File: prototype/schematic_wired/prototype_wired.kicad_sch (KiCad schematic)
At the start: 19 parts, among them J1 Conn4L, J10 LimitSwitch, J11 Conn4L, J2 Conn4L, J3 Conn4L, J4 EncoderSwitch, J5 EncoderSwitch, J6 EncoderSwitch, J7 Conn4L, J8 Conn4L, J9 LimitSwitch, U1 TMC2209-LA, U2 TMC2209-LA, U3 TMC2209-LA, U4 TCA9548A

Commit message: updates
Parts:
- removed ESP1: Conn11R, symbol Conn11R
- removed ESP2: Conn13L, symbol Conn13L
- removed J10, J9: LimitSwitch, symbol LimitSwitch
- removed J4, J5, J6: EncoderSwitch, symbol EncoderSwitch
- removed J7, J8: Conn4L, symbol Conn4L
- removed PWR1: Conn2L, symbol Conn2L
- removed U1, U2, U3: TMC2209-LA, symbol TMC2209-LA
- removed U4: TCA9548A, symbol TCA9548A
- added J12: oled, symbol Conn4L
- added J4, J5, J6: tmcA, symbol Connector_Generic:Conn_01x08
- added U1: TCA9548APWR, Package_SO:TSSOP-24_4.4x7.8mm_P0.65mm, symbol Interface_Expansion:TCA9548APWR
- added U5: ESP32-S3-DevKitC, PCM_Espressif:ESP32-S3-DevKitC, symbol PCM_Espressif:ESP32-S3-DevKitC
- J1: value Conn4L -> as5600_3
- J2: value Conn4L -> as5600_2
- J3: value Conn4L -> as5600_1
- renumbered ESP3 to 5v-in
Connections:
- new net: 5v-in.1, U5.21 (5V)
- new net: J3.1, U1.9 (SC2)
- new net: J3.2, U1.8 (SD2)
- new net: J1.3, J12.3, J2.3, J3.3, U1.24 (VCC), U1.3 (~{RESET}), U5.1 (3V3), U5.2 (3V3)
- new net: J1.4, J12.4, J2.4, J3.4, U1.1 (A0), U1.12 (GND), U1.2 (A1), U1.21 (A2), U5.22 (GND), U5.23 (GND), U5.24 (GND), U5.44 (GND)
- new net: J2.1, U1.7 (SC1)
- new net: J2.2, U1.6 (SD1)
- new net: J1.1, U1.5 (SC0)
- new net: J1.2, U1.4 (SD0)
- new net: J12.1, U5.20 (GPIO14/ADC2_CH3)
- new net: J12.2, U5.19 (GPIO13/ADC2_CH2)
- new net: U1.22 (SCL), U5.18 (GPIO12/ADC2_CH1)
- new net: U1.23 (SDA), U5.17 (GPIO11/ADC2_CH0)
- new net STEPPER_EN: J4.5 (Pin_5), J5.5 (Pin_5), J6.5 (Pin_5), U5.16 (GPIO10/ADC1_CH9)
- new net STEPPER_RX: J4.6 (Pin_6), J5.6 (Pin_6), J6.6 (Pin_6), U5.28 (GPIO47)
- new net STEPPER_TX: J4.7 (Pin_7), J5.7 (Pin_7), J6.7 (Pin_7), U5.38 (GPIO41/MTDI)
- new net encoder1_A: U5.8 (GPIO15/ADC2_CH4/32K_P)
- new net encoder1_B: U5.9 (GPIO16/ADC2_CH5/32K_N)
- new net encoder1_button: U5.10 (GPIO17/ADC2_CH6)
- new net encoder2_A: U5.11 (GPIO18/ADC2_CH7)
- new net encoder2_B: U5.27 (GPIO21)
- new net encoder2_button: U5.35 (GPIO38)
- new net encoder3_A: U5.41 (GPIO1/ADC1_CH0)
- new net encoder3_B: U5.40 (GPIO2/ADC1_CH1)
- new net encoder3_button: U5.39 (GPIO42/MTMS)
- new net tmcA_DIR: J4.1 (Pin_1), U5.5 (GPIO5/ADC1_CH4)
- new net tmcA_STEP: J4.2 (Pin_2), U5.4 (GPIO4/ADC1_CH3)
- new net tmcA_max: J4.3 (Pin_3), U5.37 (GPIO40/MTDO)
- new net tmcA_min: J4.4 (Pin_4), U5.36 (GPIO39/MTCK)
- new net tmcB_DIR: J5.1 (Pin_1), U5.7 (GPIO7/ADC1_CH6)
- new net tmcB_STEP: J5.2 (Pin_2), U5.6 (GPIO6/ADC1_CH5)
- new net tmcC_DIR: J6.1 (Pin_1), U5.15 (GPIO9/ADC1_CH8)
- new net tmcC_STEP: J6.2 (Pin_2), U5.12 (GPIO8/ADC1_CH7)
- now unconnected: 5v-in.2, J11.1, J11.2, J11.3, J11.4
- no-connect marks 38 -> 0
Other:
- note removed: "3V3 rail"
- note removed: "CLK->GND"
- note removed: "GND rail"
- note removed: "MS1->3V3 (addr1)"
- note removed: "MS1->GND (addr0)"
- note removed: "MS1->GND (addr2)"
- note removed: "MS2->3V3 (addr2)"
- note removed: "MS2->GND (addr0)"
- note removed: "MS2->GND (addr1)"
- note removed: "VM rail (12-24V, from PWR1)"
- note removed: "physical board: separate TX/RX pads, on-board resistor between them -- one node here"
- moved on the sheet: 5v-in, J1, J2, J3

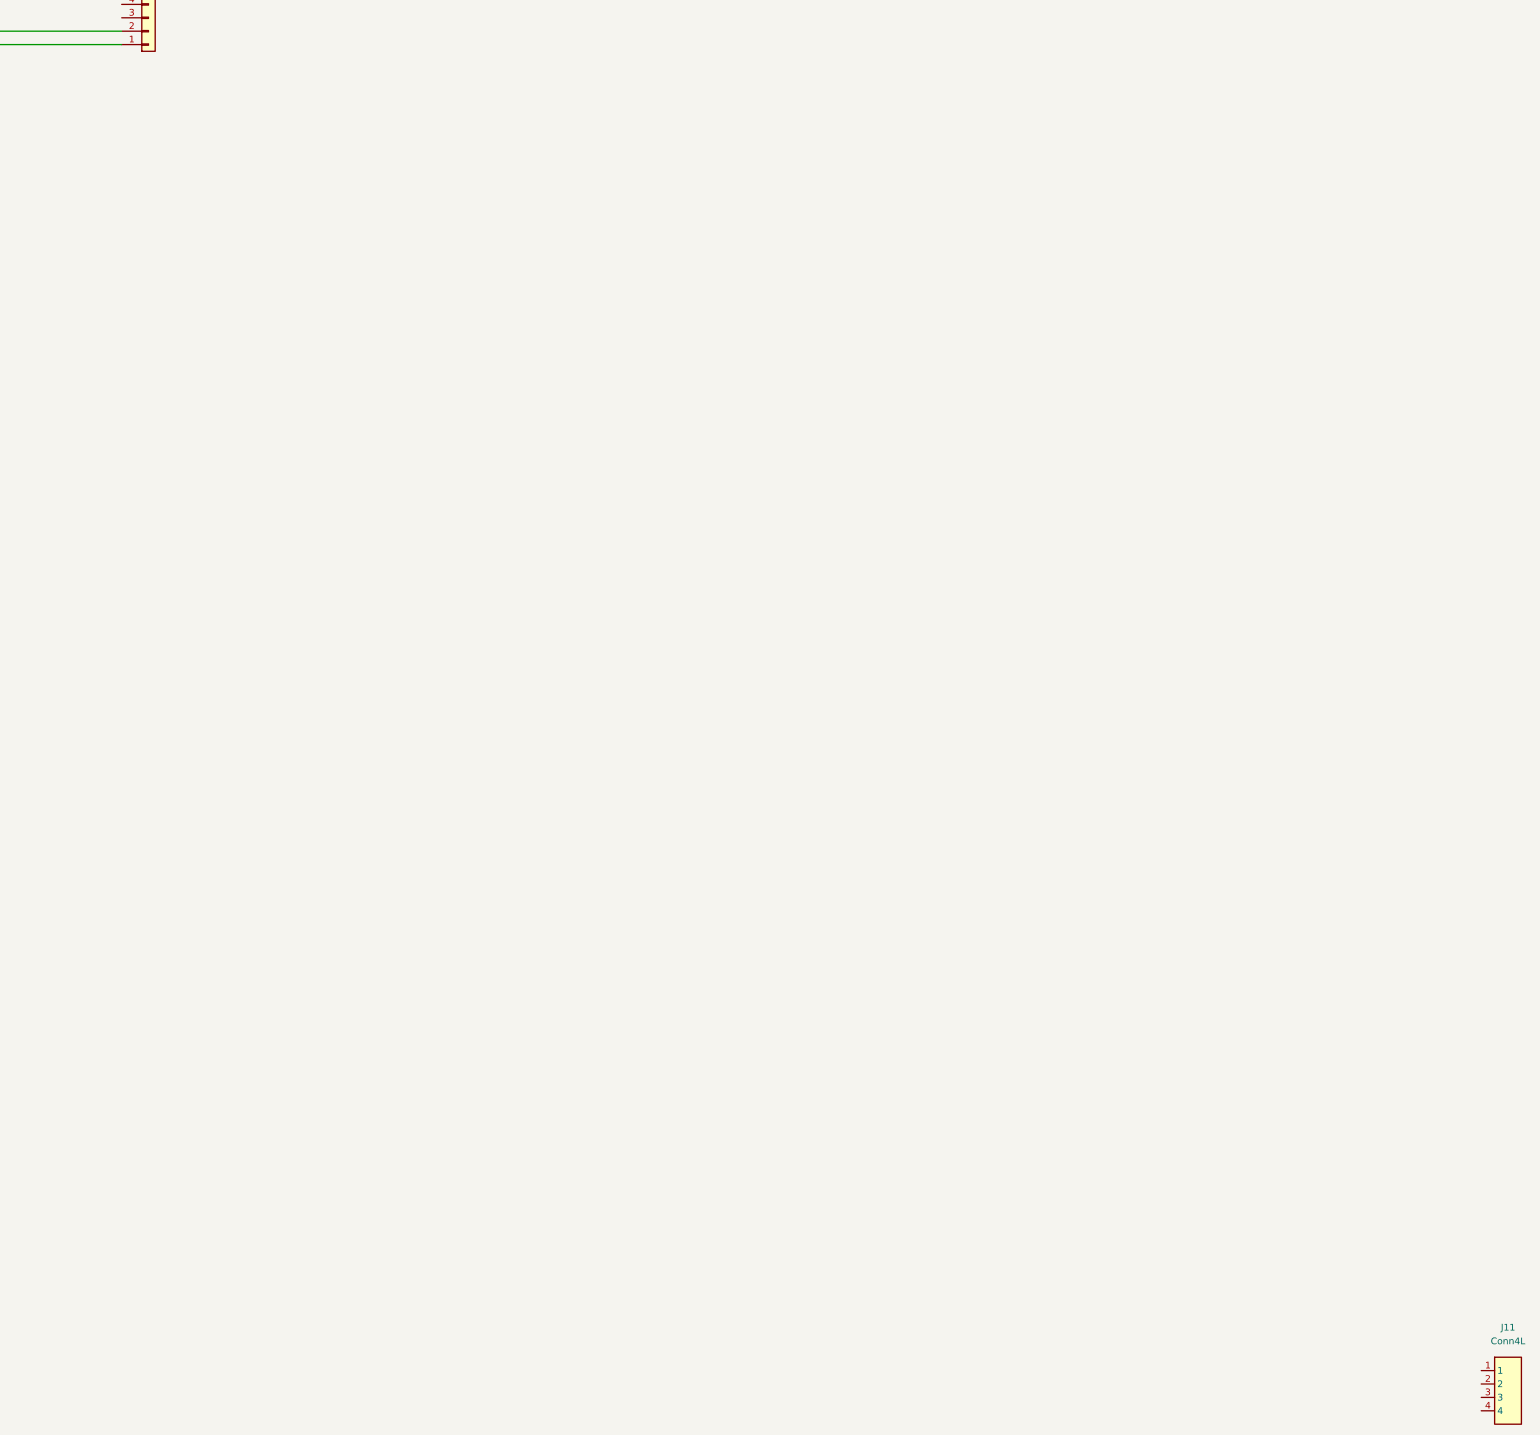
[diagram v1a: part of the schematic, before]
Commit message: fullpcb filled out
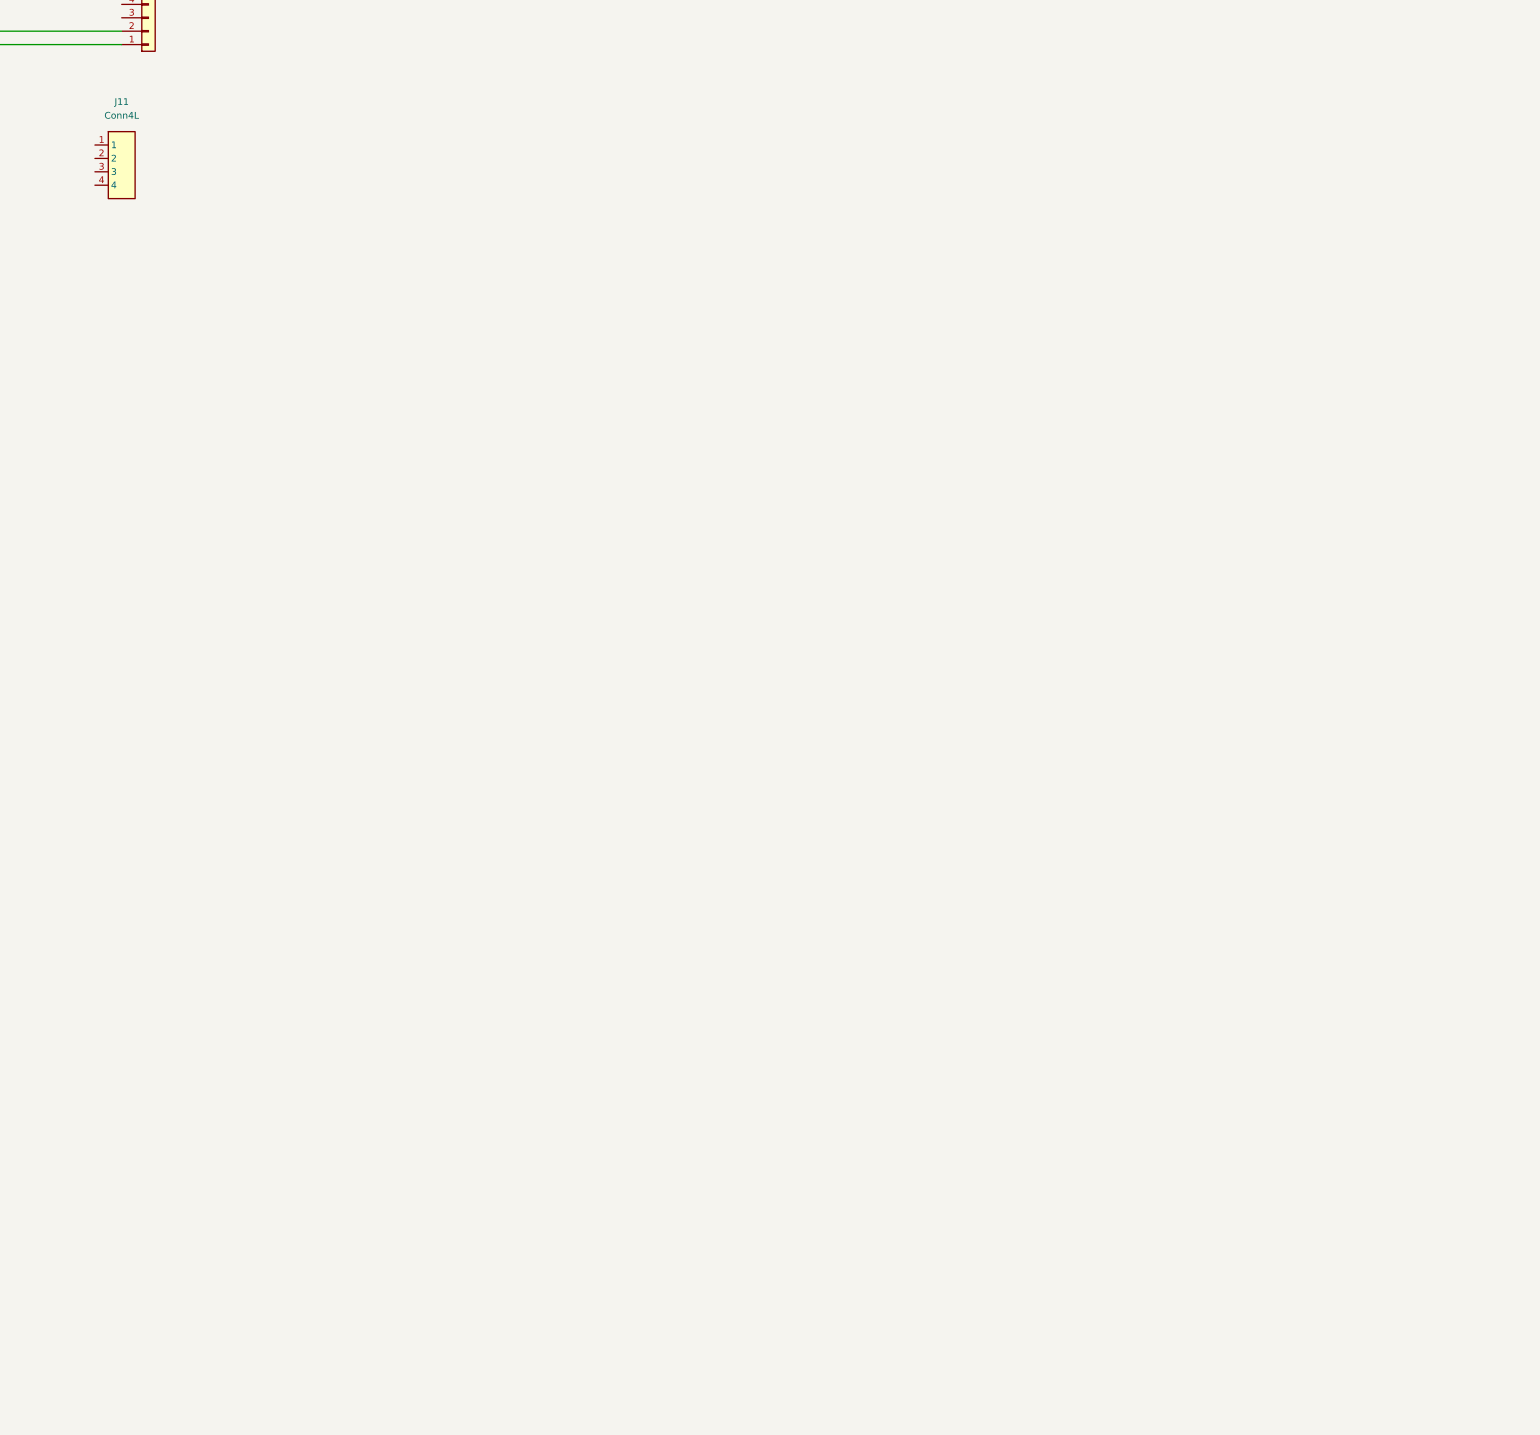
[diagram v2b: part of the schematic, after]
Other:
- moved on the sheet: J11
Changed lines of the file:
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@@
 	(symbol
 		(lib_id "Conn4L")
-		(at 560.07 439.42 0)
+		(at 297.18 207.01 0)
 		(unit 1)
 		(body_style 1)
@@
 		(fields_autoplaced yes)
 		(property "Reference" "J11"
-			(at 560.07 427.42 0)
+			(at 297.18 195.01 0)
 			(show_name no)
 			(do_not_autoplace no)
@@
 		)
 		(property "Value" "Conn4L"
-			(at 560.07 430.02 0)
+			(at 297.18 197.61 0)
 			(show_name no)
 			(do_not_autoplace no)
@@
 		)
 		(property "Footprint" ""
-			(at 560.07 439.42 0)
+			(at 297.18 207.01 0)
 			(show_name no)
 			(do_not_autoplace no)
@@
 		)
 		(property "Datasheet" ""
-			(at 560.07 439.42 0)
+			(at 297.18 207.01 0)
 			(show_name no)
 			(do_not_autoplace no)
@@
 		)
 		(property "Description" ""
-			(at 560.07 439.42 0)
+			(at 297.18 207.01 0)
 			(show_name no)
 			(do_not_autoplace no)
